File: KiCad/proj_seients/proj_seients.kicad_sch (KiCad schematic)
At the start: 0 parts

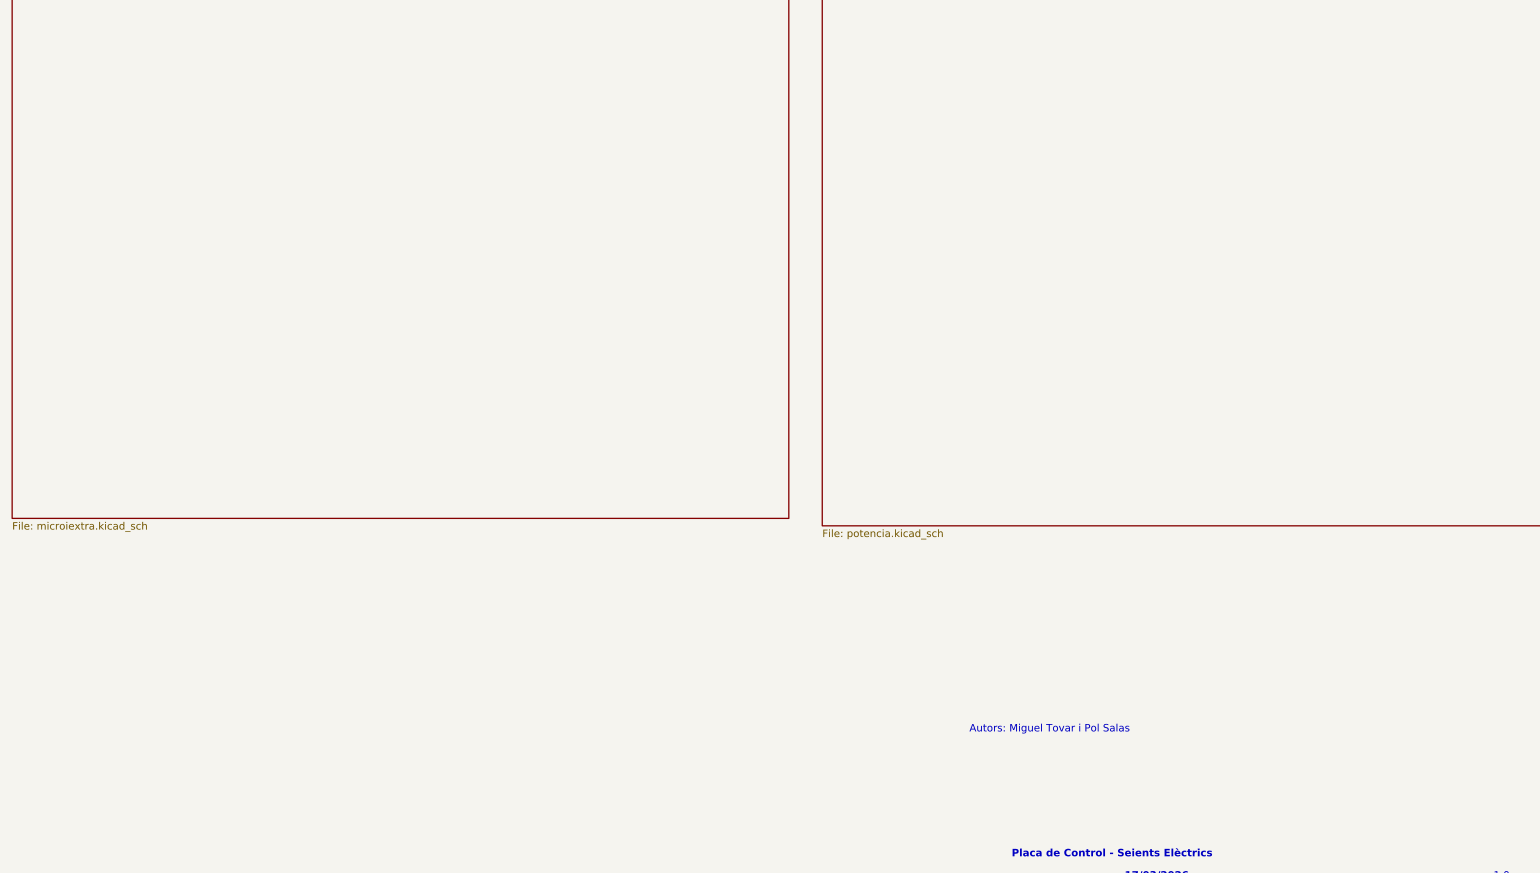
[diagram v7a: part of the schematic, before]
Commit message: Canvi de TCAN i Afegit CAN DE.9
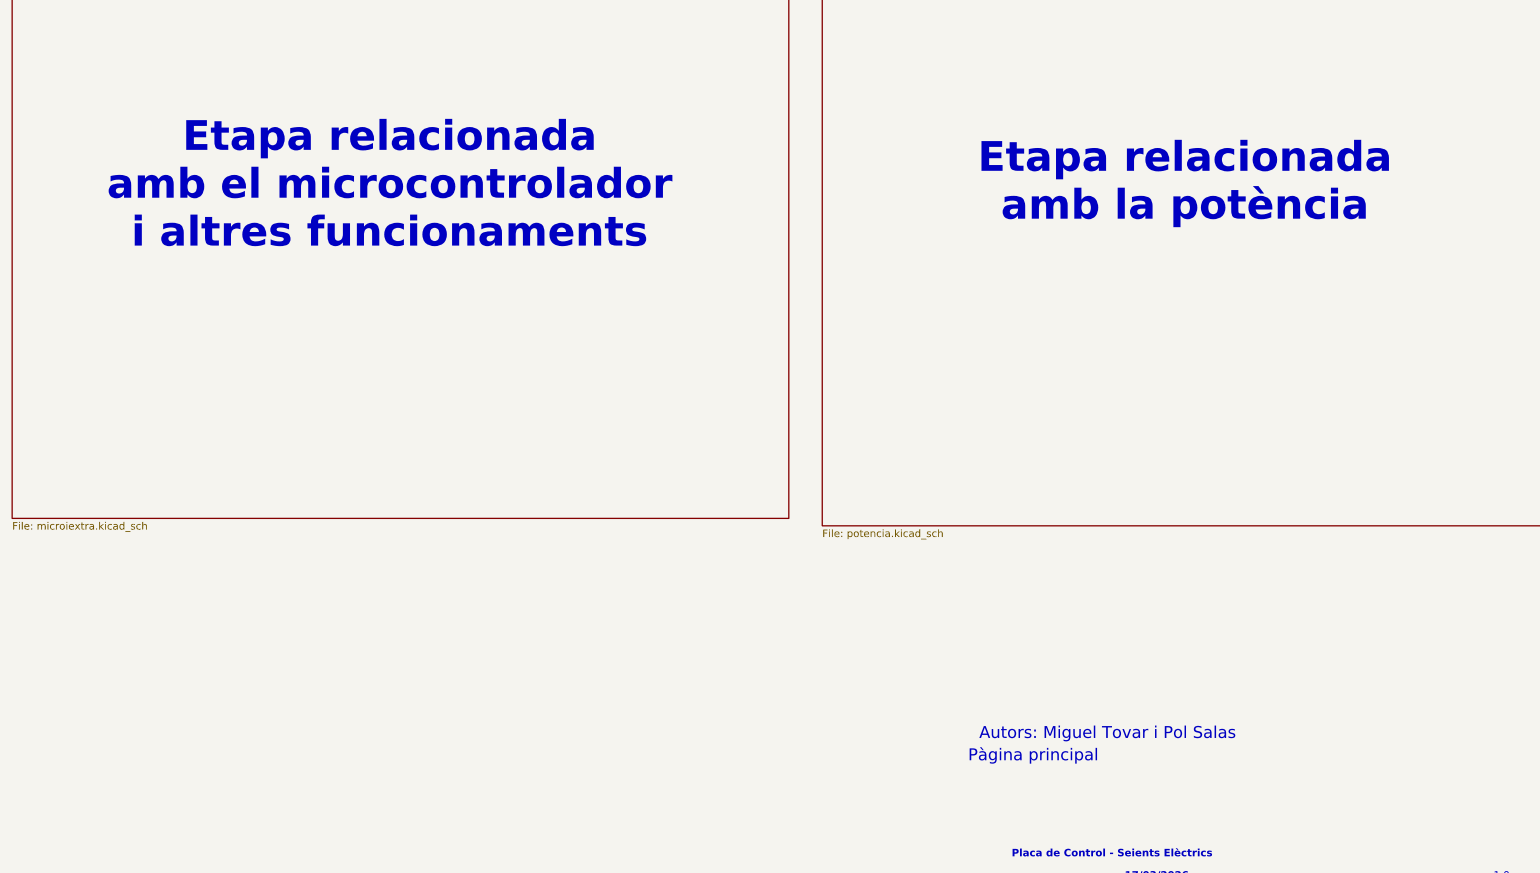
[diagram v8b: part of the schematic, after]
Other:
- note added: "Etapa relacionada amb el microcontrolador i altres funcionaments"
- note added: "Etapa relacionada amb la potència"
- note added: "Pàgina principal"
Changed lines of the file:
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@@
+		)
+	)
+	(text "Etapa relacionada \namb el microcontrolador \ni altres funcionaments"
+		(exclude_from_sim no)
+		(at 81.026 75.184 0)
+		(effects
+			(font
+				(size 5.08 5.08)
+				(thickness 0.762)
+				(bold yes)
+			)
 		)
 	)
@@
 				(size 1.27 1.27)
 				(thickness 0.254)
+				(bold yes)
+			)
+		)
+	)
+	(text "Etapa relacionada \namb la potència"
+		(exclude_from_sim no)
+		(at 216.916 74.676 0)
+		(effects
+			(font
+				(size 5.08 5.08)
+				(thickness 0.762)
 				(bold yes)
 			)
@@
 		)
 	)
+	(text "Pàgina principal"
+		(exclude_from_sim no)
+		(at 191.008 172.72 0)
+		(effects
+			(font
+				(size 2.032 2.032)
+				(thickness 0.254)
+			)
+		)
+	)
 	(text "Autors: Miguel Tovar i Pol Salas"
 		(exclude_from_sim no)
-		(at 193.802 168.148 0)
+		(at 203.708 168.91 0)
 		(effects
 			(font
-				(size 1.27 1.27)
+				(size 2.032 2.032)
 			)
 		)
